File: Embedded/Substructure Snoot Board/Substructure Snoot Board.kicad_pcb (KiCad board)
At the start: 4 copper layers, 50 x 35 mm, 23 parts, among them J3 L0 JST, J4 L1 JST, J6 A JST, J7 S Pins A, J8 S Pins B, U1 D0 FFC, U2 D1 FFC, U3 U FFC, U4 S FFC, U5 R FFC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

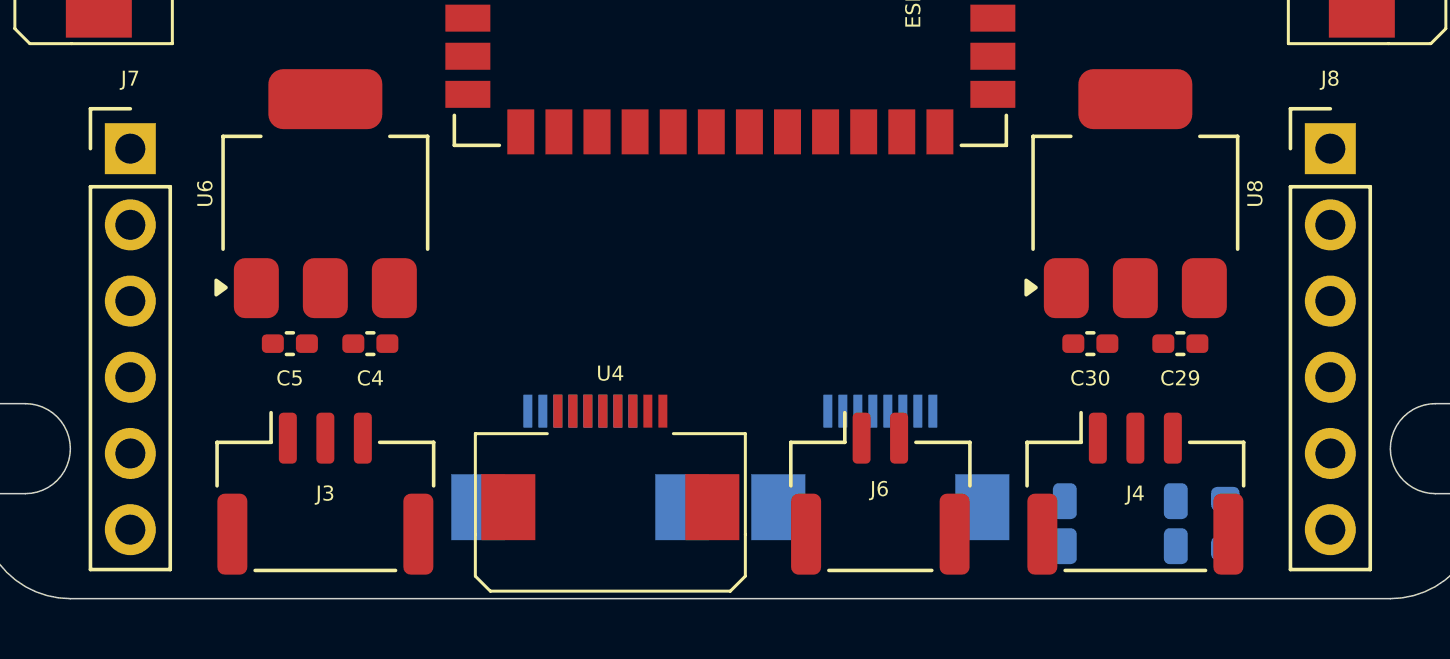
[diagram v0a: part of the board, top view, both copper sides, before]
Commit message: Added System PWR Jumper Pins & USBC Connector & PWR Indicator LEDS
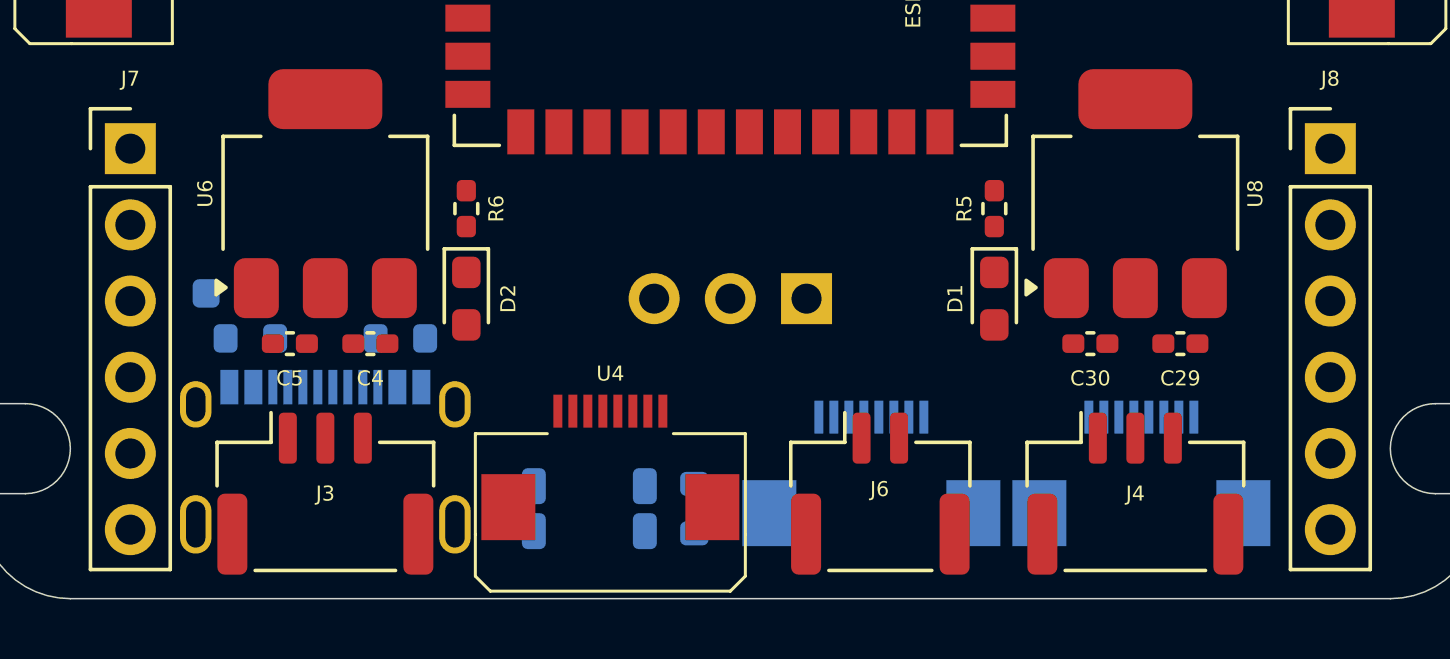
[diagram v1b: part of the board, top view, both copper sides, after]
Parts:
- added C6: 10uF, Capacitor_SMD:C_0603_1608Metric, B.Cu at (93.3, 69.8)
- added D1: LED, Diode_SMD:D_0603_1608Metric_Pad1.05x0.95mm_HandSolder, F.Cu at (118.8, 70.0)
- added D2: LED, Diode_SMD:D_0603_1608Metric_Pad1.05x0.95mm_HandSolder, F.Cu at (101.2, 70.0)
- added J1: 10171746-00021LF, USBC:AMPHENOL_10171746-00021LF, B.Cu at (96.5, 77.5)
- added J2: PWR Jumper Pins, Connector_PinHeader_2.54mm:PinHeader_1x03_P2.54mm_Horizontal, B.Cu at (112.5, 70.0)
- added R3: 5.1K, Resistor_SMD:R_0603_1608Metric, B.Cu at (94.0, 71.3)
- added R4: 5.1K, Resistor_SMD:R_0603_1608Metric, B.Cu at (99.0, 71.3)
- added R5: 155ohm min, Resistor_SMD:R_0402_1005Metric_Pad0.72x0.64mm_HandSolder, F.Cu at (118.8, 67.0)
- added R6: 70ohm min, Resistor_SMD:R_0402_1005Metric_Pad0.72x0.64mm_HandSolder, F.Cu at (101.2, 67.0)
- moved U3 18.7 mm to (123.7, 74.6)
- moved BootSW1 17.7 mm to (105.3, 77.0)
- moved R2 17.7 mm to (108.8, 77.0)
- moved U5 0.36 mm to (114.7, 74.6)
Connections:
- C4 pad 1: +RAWVS -> +PWR
- U6 pad 3: +RAWVS -> +PWR

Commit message: Added RST Button
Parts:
- added RstSW1: SW_Push, Buttons:R-667843, B.Cu at (104.0, 76.5)
- moved R2 4.08 mm to (108.0, 73.0), turned to 0 degrees
- moved BootSW1 2.75 mm to (108.0, 76.5), turned to -90 degrees
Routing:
- added copper zone on B.Cu, net +5V
- added copper zone on F.Cu, net +5V
- added copper zone on In1.Cu, net GND
- added copper zone on In2.Cu, net GND
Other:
- outline, holes or cut-outs redrawn

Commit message: Added Enable Pins to PSU Connector
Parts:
- added R7: 5.1K, Resistor_SMD:R_0603_1608Metric, B.Cu at (127.9, 71.8)
- added R8: 5.1K, Resistor_SMD:R_0603_1608Metric, B.Cu at (127.9, 68.8)
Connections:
- J8 pad 2: GND -> Net-(J8-Pin_2)
- J8 pad 5: GND -> Net-(J8-Pin_5)

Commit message: Modified S Pins to Mill Max
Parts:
- J7, J8: footprint Connector_PinHeader_2.54mm:PinHeader_1x06_P2.54mm_Vertical -> Connector_PinSocket_2.54mm:PinSocket_1x06_P2.54mm_Vertical
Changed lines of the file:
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@@
 		)
 	)
-	(footprint "Connector_PinHeader_2.54mm:PinHeader_1x06_P2.54mm_Vertical"
+	(footprint "Connector_PinSocket_2.54mm:PinSocket_1x06_P2.54mm_Vertical"
 		(layer "F.Cu")
 		(at 130 65)
-		(descr "Through hole straight pin header, 1x06, 2.54mm pitch, single row")
-		(tags "Through hole pin header THT 1x06 2.54mm single row")
+		(descr "Through hole straight socket strip, 1x06, 2.54mm pitch, single row (from Kicad 4.0.7), script generated")
+		(tags "Through hole socket strip THT 1x06 2.54mm single row")
 		(property "Reference" "J8"
-			(at 0 -2.33 0)
+			(at 0 -2.5 0)
 			(layer "F.SilkS")
 			(effects
 				(font
 					(size 0.5 0.5)
-					(thickness 0.15)
+					(thickness 0.125)
 				)
 			)
 		)
 		(property "Value" "S Pins B"
-			(at 0 15.03 0)
-			(layer "F.Fab")
-			(hide yes)
-			(effects
-				(font
-					(size 0.5 0.5)
-					(thickness 0.15)
-				)
-			)
-		)
-		(property "Footprint" "Connector_PinHeader_2.54mm:PinHeader_1x06_P2.54mm_Vertical"
+			(at 0 15.47 0)
+			(layer "F.Fab")
+			(hide yes)
+			(effects
+				(font
+					(size 1 1)
+					(thickness 0.15)
+				)
+			)
+		)
+		(property "Footprint" "Connector_PinSocket_2.54mm:PinSocket_1x06_P2.54mm_Vertical"
 			(at 0 0 0)
 			(unlocked yes)
@@
 		(attr through_hole)
 		(fp_line
-			(start -1.33 -1.33)
-			(end 0 -1.33)
-			(stroke
-				(width 0.12)
-				(type solid)
-			)
-			(layer "F.SilkS")
-		)
-		(fp_line
-			(start -1.33 0)
-			(end -1.33 -1.33)
-			(stroke
-				(width 0.12)
-				(type solid)
-			)
-			(layer "F.SilkS")
-		)
-		(fp_line
 			(start -1.33 1.27)
 			(end -1.33 14.03)
@@
 		)
 		(fp_line
+			(start 0 -1.33)
+			(end 1.33 -1.33)
+			(stroke
+				(width 0.12)
+				(type solid)
+			)
+			(layer "F.SilkS")
+		)
+		(fp_line
+			(start 1.33 -1.33)
+			(end 1.33 0)
+			(stroke
+				(width 0.12)
+				(type solid)
+			)
+			(layer "F.SilkS")
+		)
+		(fp_line
 			(start 1.33 1.27)
 			(end 1.33 14.03)
@@
 		(fp_line
 			(start -1.8 -1.8)
-			(end -1.8 14.5)
-			(stroke
-				(width 0.05)
-				(type solid)
-			)
-			(layer "F.CrtYd")
-		)
-		(fp_line
-			(start -1.8 14.5)
-			(end 1.8 14.5)
-			(stroke
-				(width 0.05)
-				(type solid)
-			)
-			(layer "F.CrtYd")
-		)
-		(fp_line
-			(start 1.8 -1.8)
+			(end 1.75 -1.8)
+			(stroke
+				(width 0.05)
+				(type solid)
+			)
+			(layer "F.CrtYd")
+		)
+		(fp_line
+			(start -1.8 14.45)
 			(end -1.8 -1.8)
 			(stroke
@@
 		)
 		(fp_line
-			(start 1.8 14.5)
-			(end 1.8 -1.8)
-			(stroke
-				(width 0.05)
-				(type solid)
-			)
-			(layer "F.CrtYd")
-		)
-		(fp_line
-			(start -1.27 -0.635)
-			(end -0.635 -1.27)
+			(start 1.75 -1.8)
+			(end 1.75 14.45)
+			(stroke
+				(width 0.05)
+				(type solid)
+			)
+			(layer "F.CrtYd")
+		)
+		(fp_line
+			(start 1.75 14.45)
+			(end -1.8 14.45)
+			(stroke
+				(width 0.05)
+				(type solid)
+			)
+			(layer "F.CrtYd")
+		)
+		(fp_line
+			(start -1.27 -1.27)
+			(end 0.635 -1.27)
 			(stroke
 				(width 0.1)
@@
 		(fp_line
 			(start -1.27 13.97)
-			(end -1.27 -0.635)
-			(stroke
-				(width 0.1)
-				(type solid)
-			)
-			(layer "F.Fab")
-		)
-		(fp_line
-			(start -0.635 -1.27)
-			(end 1.27 -1.27)
-			(stroke
-				(width 0.1)
-				(type solid)
-			)
-			(layer "F.Fab")
-		)
-		(fp_line
-			(start 1.27 -1.27)
+			(end -1.27 -1.27)
+			(stroke
+				(width 0.1)
+				(type solid)
+			)
+			(layer "F.Fab")
+		)
+		(fp_line
+			(start 0.635 -1.27)
+			(end 1.27 -0.635)
+			(stroke
+				(width 0.1)
+				(type solid)
+			)
+			(layer "F.Fab")
+		)
+		(fp_line
+			(start 1.27 -0.635)
 			(end 1.27 13.97)
 			(stroke
@@
 			(at 0 6.35 90)
 			(layer "F.Fab")
-			(hide yes)
-			(effects
-				(font
-					(size 0.5 0.5)
+			(effects
+				(font
+					(size 1 1)
 					(thickness 0.15)
 				)
@@
 			(pintype "passive")
 		)
-		(model "${KICAD8_3DMODEL_DIR}/Connector_PinHeader_2.54mm.3dshapes/PinHeader_1x06_P2.54mm_Vertical.wrl"
+		(model "${KICAD8_3DMODEL_DIR}/Connector_PinSocket_2.54mm.3dshapes/PinSocket_1x06_P2.54mm_Vertical.wrl"
+			(hide yes)
 			(offset
 				(xyz 0 0 0)
@@
 			(rotate
 				(xyz 0 0 0)
+			)
+		)
+		(model "${KICAD8_3DMODEL_DIR}/Custom/801-xx-006-10-012000.STEP"
+			(offset
+				(xyz 0 0 2.5)
+			)
+			(scale
+				(xyz 1 1 1)
+			)
+			(rotate
+				(xyz -90 0 90)
 			)
 		)
@@
 		)
 	)
-	(footprint "Connector_PinHeader_2.54mm:PinHeader_1x06_P2.54mm_Vertical"
+	(footprint "Connector_PinSocket_2.54mm:PinSocket_1x06_P2.54mm_Vertical"
 		(layer "F.Cu")
 		(at 90 65)
-		(descr "Through hole straight pin header, 1x06, 2.54mm pitch, single row")
-		(tags "Through hole pin header THT 1x06 2.54mm single row")
+		(descr "Through hole straight socket strip, 1x06, 2.54mm pitch, single row (from Kicad 4.0.7), script generated")
+		(tags "Through hole socket strip THT 1x06 2.54mm single row")
 		(property "Reference" "J7"
-			(at 0 -2.33 0)
+			(at 0 -2.5 0)
 			(layer "F.SilkS")
 			(effects
 				(font
 					(size 0.5 0.5)
-					(thickness 0.15)
+					(thickness 0.125)
 				)
 			)
 		)
 		(property "Value" "S Pins A"
-			(at 0 15.03 0)
-			(layer "F.Fab")
-			(hide yes)
-			(effects
-				(font
-					(size 0.5 0.5)
-					(thickness 0.15)
-				)
-			)
-		)
-		(property "Footprint" "Connector_PinHeader_2.54mm:PinHeader_1x06_P2.54mm_Vertical"
+			(at 0 15.47 0)
+			(layer "F.Fab")
+			(hide yes)
+			(effects
+				(font
+					(size 1 1)
+					(thickness 0.15)
+				)
+			)
+		)
+		(property "Footprint" "Connector_PinSocket_2.54mm:PinSocket_1x06_P2.54mm_Vertical"
 			(at 0 0 0)
 			(unlocked yes)
@@
 		(attr through_hole)
 		(fp_line
-			(start -1.33 -1.33)
-			(end 0 -1.33)
-			(stroke
-				(width 0.12)
-				(type solid)
-			)
-			(layer "F.SilkS")
-		)
-		(fp_line
-			(start -1.33 0)
-			(end -1.33 -1.33)
-			(stroke
-				(width 0.12)
-				(type solid)
-			)
-			(layer "F.SilkS")
-		)
-		(fp_line
 			(start -1.33 1.27)
 			(end -1.33 14.03)
@@
 		)
 		(fp_line
+			(start 0 -1.33)
+			(end 1.33 -1.33)
+			(stroke
+				(width 0.12)
+				(type solid)
+			)
+			(layer "F.SilkS")
+		)
+		(fp_line
+			(start 1.33 -1.33)
+			(end 1.33 0)
+			(stroke
+				(width 0.12)
+				(type solid)
+			)
+			(layer "F.SilkS")
+		)
+		(fp_line
 			(start 1.33 1.27)
 			(end 1.33 14.03)
@@
 		(fp_line
 			(start -1.8 -1.8)
-			(end -1.8 14.5)
-			(stroke
-				(width 0.05)
-				(type solid)
-			)
-			(layer "F.CrtYd")
-		)
-		(fp_line
-			(start -1.8 14.5)
-			(end 1.8 14.5)
-			(stroke
-				(width 0.05)
-				(type solid)
-			)
-			(layer "F.CrtYd")
-		)
-		(fp_line
-			(start 1.8 -1.8)
+			(end 1.75 -1.8)
+			(stroke
+				(width 0.05)
+				(type solid)
+			)
+			(layer "F.CrtYd")
+		)
+		(fp_line
+			(start -1.8 14.45)
 			(end -1.8 -1.8)
 			(stroke
@@
 		)
 		(fp_line
-			(start 1.8 14.5)
-			(end 1.8 -1.8)
-			(stroke
-				(width 0.05)
-				(type solid)
-			)
-			(layer "F.CrtYd")
-		)
-		(fp_line
-			(start -1.27 -0.635)
-			(end -0.635 -1.27)
+			(start 1.75 -1.8)
+			(end 1.75 14.45)
+			(stroke
+				(width 0.05)
+				(type solid)
+			)
+			(layer "F.CrtYd")
+		)
+		(fp_line
+			(start 1.75 14.45)
+			(end -1.8 14.45)
+			(stroke
+				(width 0.05)
+				(type solid)
+			)
+			(layer "F.CrtYd")
+		)
+		(fp_line
+			(start -1.27 -1.27)
+			(end 0.635 -1.27)
 			(stroke
 				(width 0.1)
@@
 		(fp_line
 			(start -1.27 13.97)
-			(end -1.27 -0.635)
-			(stroke
-				(width 0.1)
-				(type solid)
-			)
-			(layer "F.Fab")
-		)
-		(fp_line
-			(start -0.635 -1.27)
-			(end 1.27 -1.27)
-			(stroke
-				(width 0.1)
-				(type solid)
-			)
-			(layer "F.Fab")
-		)
-		(fp_line
-			(start 1.27 -1.27)
+			(end -1.27 -1.27)
+			(stroke
+				(width 0.1)
+				(type solid)
+			)
+			(layer "F.Fab")
+		)
+		(fp_line
+			(start 0.635 -1.27)
+			(end 1.27 -0.635)
+			(stroke
+				(width 0.1)
+				(type solid)
+			)
+			(layer "F.Fab")
+		)
+		(fp_line
+			(start 1.27 -0.635)
 			(end 1.27 13.97)
 			(stroke
@@
 			(at 0 6.35 90)
 			(layer "F.Fab")
-			(hide yes)
-			(effects
-				(font
-					(size 0.5 0.5)
+			(effects
+				(font
+					(size 1 1)
 					(thickness 0.15)
 				)
@@
 			(pintype "passive")
 		)
-		(model "${KICAD8_3DMODEL_DIR}/Connector_PinHeader_2.54mm.3dshapes/PinHeader_1x06_P2.54mm_Vertical.wrl"
+		(model "${KICAD8_3DMODEL_DIR}/Connector_PinSocket_2.54mm.3dshapes/PinSocket_1x06_P2.54mm_Vertical.wrl"
+			(hide yes)
 			(offset
 				(xyz 0 0 0)
@@
 			)
 		)
+		(model "${KICAD8_3DMODEL_DIR}/Custom/801-xx-006-10-012000.STEP"
+			(offset
+				(xyz 0 0 2.5)
+			)
+			(scale
+				(xyz 1 1 1)
+			)
+			(rotate
+				(xyz -90 0 90)
+			)
+		)

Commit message: Added Extra Power Pads to the Bottom
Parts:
- added J5: 5Vout, TestPoint:TestPoint_Pad_D4.0mm, B.Cu at (117.5, 67.5)
- added J9: GNDout, TestPoint:TestPoint_Pad_D4.0mm, B.Cu at (102.5, 67.5)
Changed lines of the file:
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@@
+		)
+	)
+	(footprint "TestPoint:TestPoint_Pad_D4.0mm"
+		(layer "B.Cu")
+		(at 117.5 67.5 180)
+		(descr "SMD pad as test Point, diameter 4.0mm")
+		(tags "test point SMD pad")
+		(property "Reference" "J5"
+			(at 0 2.898 0)
+			(layer "B.SilkS")
+			(hide yes)
+			(effects
+				(font
+					(size 1 1)
+					(thickness 0.15)
+				)
+				(justify mirror)
+			)
+		)
+		(property "Value" "5Vout"
+			(at 0 3.25 0)
+			(layer "B.SilkS")
+			(effects
+				(font
+					(size 1 1)
+					(thickness 0.15)
+				)
+				(justify mirror)
+			)
+		)
+		(property "Footprint" "TestPoint:TestPoint_Pad_D4.0mm"
+			(at 0 0 0)
+			(unlocked yes)
+			(layer "B.Fab")
+			(hide yes)
+			(effects
+				(font
+					(size 1.27 1.27)
+					(thickness 0.15)
+				)
+				(justify mirror)
+			)
+		)
+		(property "Datasheet" ""
+			(at 0 0 0)
+			(unlocked yes)
+			(layer "B.Fab")
+			(hide yes)
+			(effects
+				(font
+					(size 1.27 1.27)
+					(thickness 0.15)
+				)
+				(justify mirror)
+			)
+		)
+		(property "Description" "Generic connector, single row, 01x01, script generated"
+			(at 0 0 0)
+			(unlocked yes)
+			(layer "B.Fab")
+			(hide yes)
+			(effects
+				(font
+					(size 1.27 1.27)
+					(thickness 0.15)
+				)
+				(justify mirror)
+			)
+		)
+		(property ki_fp_filters "Connector*:*_1x??_*")
+		(sheetname "Root")
+		(sheetfile "Substructure Snoot Board.kicad_sch")
+		(attr exclude_from_pos_files)
+		(fp_circle
+			(center 0 0)
+			(end 0 -2.25)
+			(stroke
+				(width 0.12)
+				(type solid)
+			)
+			(fill none)
+			(layer "B.SilkS")
+		)
+		(fp_circle
+			(center 0 0)
+			(end 2.5 0)
+			(stroke
+				(width 0.05)
+				(type solid)
+			)
+			(fill none)
+			(layer "B.CrtYd")
+		)
+		(pad "1" smd circle
+			(at 0 0 180)
+			(size 4 4)
+			(layers "B.Cu" "B.Mask")
+			(net 40 "+5V")
+			(pinfunction "Pin_1")
+			(pintype "passive")
 		)
 	)
@@
 		)
 	)
+	(footprint "TestPoint:TestPoint_Pad_D4.0mm"
+		(layer "B.Cu")
+		(at 102.5 67.5 180)
+		(descr "SMD pad as test Point, diameter 4.0mm")
+		(tags "test point SMD pad")
+		(property "Reference" "J9"
+			(at 0 2.898 0)
+			(layer "B.SilkS")
+			(hide yes)
+			(effects
+				(font
+					(size 1 1)
+					(thickness 0.15)
+				)
+				(justify mirror)
+			)
+		)
+		(property "Value" "GNDout"
+			(at 0 3.25 0)
+			(layer "B.SilkS")
+			(effects
+				(font
+					(size 1 1)
+					(thickness 0.15)
+				)
+				(justify mirror)
+			)
+		)
+		(property "Footprint" "TestPoint:TestPoint_Pad_D4.0mm"
+			(at 0 0 0)
+			(unlocked yes)
+			(layer "B.Fab")
+			(hide yes)
+			(effects
+				(font
+					(size 1.27 1.27)
+					(thickness 0.15)
+				)
+				(justify mirror)
+			)
+		)
+		(property "Datasheet" ""
+			(at 0 0 0)
+			(unlocked yes)
+			(layer "B.Fab")
+			(hide yes)
+			(effects
+				(font
+					(size 1.27 1.27)
+					(thickness 0.15)
+				)
+				(justify mirror)
+			)
+		)
+		(property "Description" "Generic connector, single row, 01x01, script generated"
+			(at 0 0 0)
+			(unlocked yes)
+			(layer "B.Fab")
+			(hide yes)
+			(effects
+				(font
+					(size 1.27 1.27)
+					(thickness 0.15)
+				)
+				(justify mirror)
+			)
+		)
+		(property ki_fp_filters "Connector*:*_1x??_*")
+		(sheetname "Root")
+		(sheetfile "Substructure Snoot Board.kicad_sch")
+		(attr exclude_from_pos_files)
+		(fp_circle
+			(center 0 0)
+			(end 0 -2.25)
+			(stroke
+				(width 0.12)
+				(type solid)
+			)
+			(fill none)
+			(layer "B.SilkS")
+		)
+		(fp_circle
+			(center 0 0)
+			(end 2.5 0)
+			(stroke
+				(width 0.05)
+				(type solid)
+			)
+			(fill none)
+			(layer "B.CrtYd")
+		)
+		(pad "1" smd circle
+			(at 0 0 180)
+			(size 4 4)
+			(layers "B.Cu" "B.Mask")
+			(net 2 "GND")
+			(pinfunction "Pin_1")
+			(pintype "passive")
+		)
+	)
